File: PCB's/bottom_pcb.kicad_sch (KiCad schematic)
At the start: 0 parts

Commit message: pcb
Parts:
- added U6: BMP581, QFN10_BMP581_BOS, symbol Library:BMP581
- added U7: SHT45-AD1F-R2, SHT45-AD1F-R2:SHT4X, symbol Library:SHT45-AD1F-R2
- added U8: SGP41-D-R4, SGP41-D-R4:XDCR_SGP41-D-R4, symbol Library:SGP41-D-R4

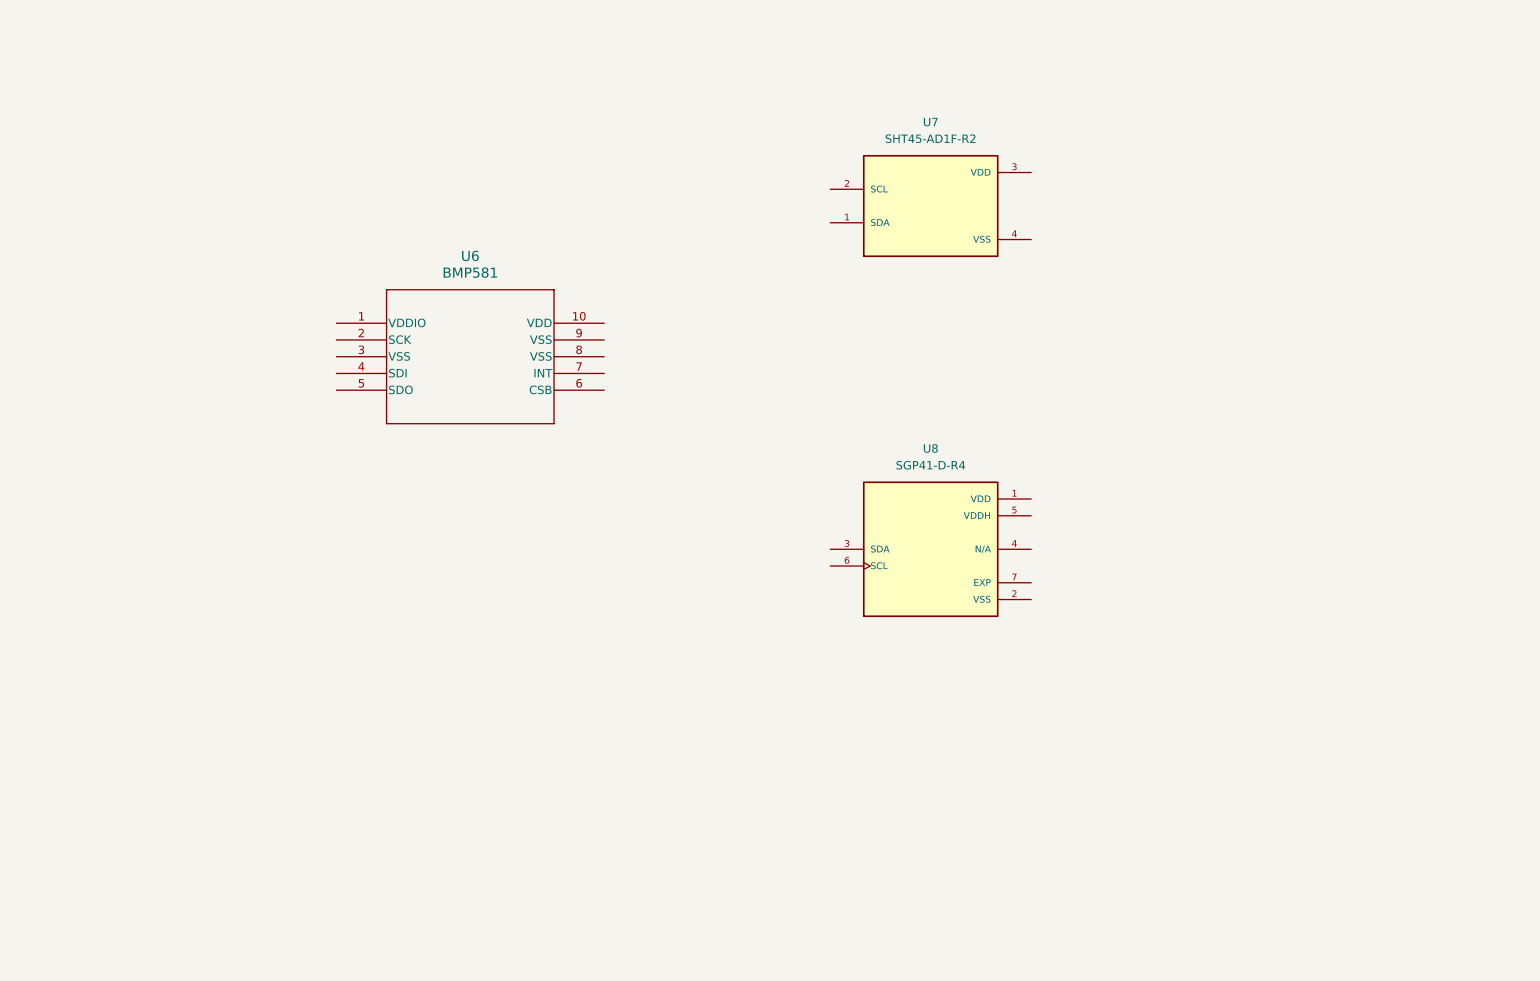
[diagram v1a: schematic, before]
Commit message: added comments and finished the bottom pcb schematics
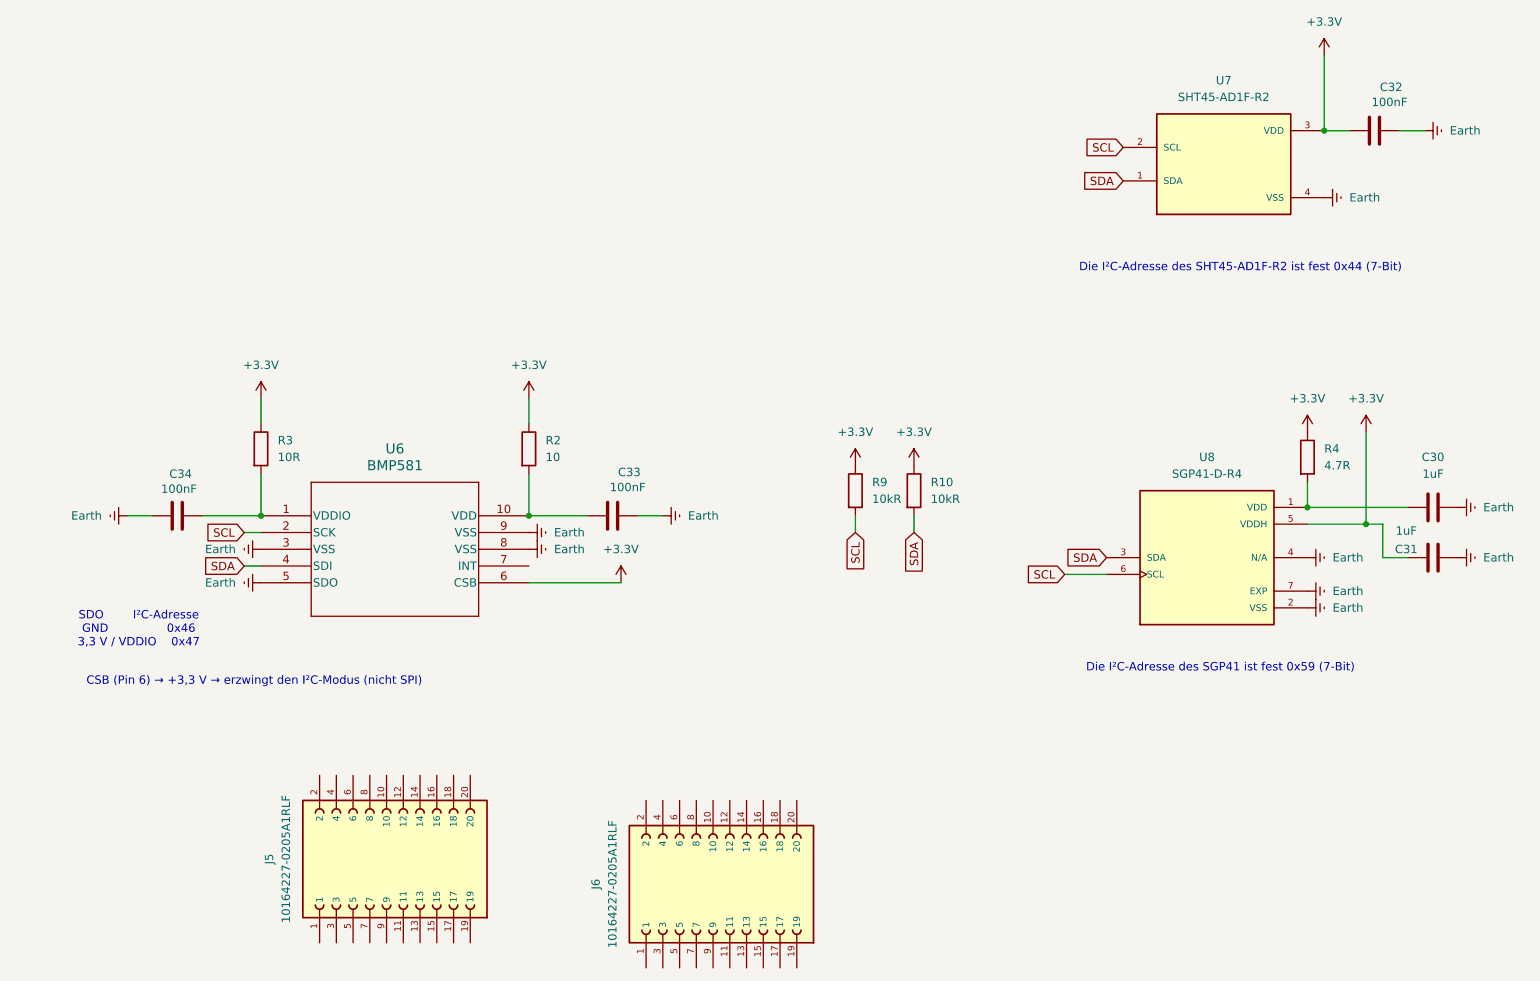
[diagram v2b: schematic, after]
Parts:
- added C30, C31: 1uF, symbol Device:C
- added C32, C33, C34: 100nF, symbol Device:C
- added J5, J6: 10164227-0205A1RLF, 10164227-0205A1RLF:AMPHENOL_10164227-0205A1RLF, symbol Library:10164227-0205A1RLF
- added R10, R9: 10kR, symbol Device:R
- added R2: 10, symbol Device:R
- added R3: 10R, symbol Device:R
- added R4: 4.7R, symbol Device:R
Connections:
- net SDA: now reaches U7.1 (SDA)
- net SDA: now also U6.4 (SDI), U8.3 (SDA), R10.2
- net SCL: now reaches U7.2 (SCL)
- net SCL: now also U6.2 (SCK), U8.6 (SCL), R9.2
- net +3.3V: now reaches U7.3 (VDD)
- net +3.3V: now also U6.6 (CSB), U8.5 (VDDH), C31.1, C32.1, R10.1, R2.1, R3.1, R4.1, R9.1
- net Earth: now reaches U7.4 (VSS)
- net Earth: now also U6.3 (VSS), U6.5 (SDO), U6.8 (VSS), U6.9 (VSS), U8.2 (VSS), U8.4 (N/A), U8.7 (EXP), C30.2, C31.2, C32.2, C33.2, C34.2
- net at U6.1 (VDDIO): now also C34.1, R3.2
- net at U6.10 (VDD): now also C33.1, R2.2
- net at U8.1 (VDD): now also C30.1, R4.2
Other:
- note added: "CSB (Pin 6) → +3,3 V → erzwingt den I²C-Modus (nicht SPI)"
- note added: "Die I²C-Adresse des SGP41 ist fest 0x59 (7-Bit)"
- note added: "Die I²C-Adresse des SHT45-AD1F-R2 ist fest 0x44 (7-Bit)"
- note added: "SDO I²C-Adresse GND 0x46 3,3 V / VDDIO 0x47"
- moved on the sheet: U6, U7, U8
